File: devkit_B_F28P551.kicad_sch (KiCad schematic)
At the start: 4 parts, among them J1 DEVKIT_C2000_ROW_A, J2 DEVKIT_C2000_ROW_B, J3 JTAG_CTBP_10, U1 TMS320F28P551SG5PM

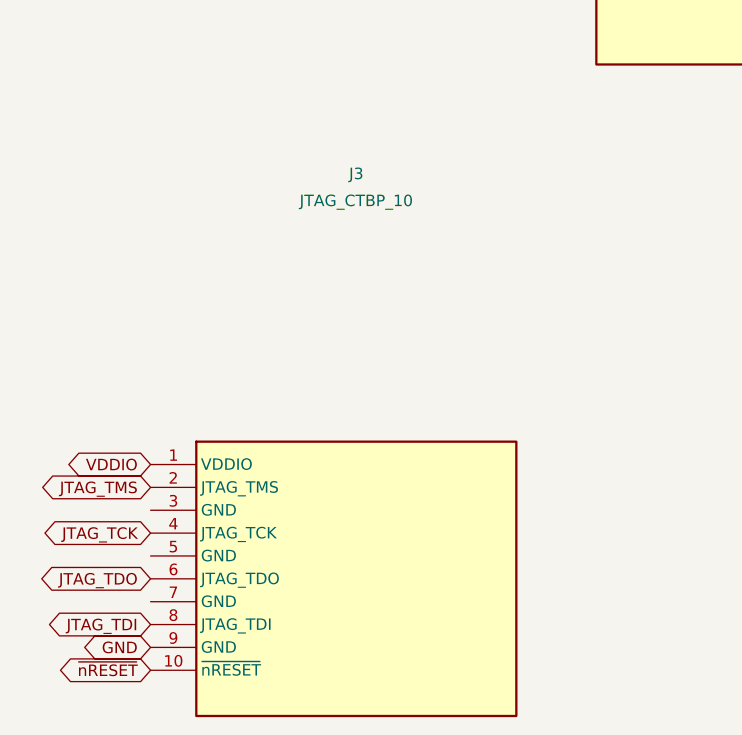
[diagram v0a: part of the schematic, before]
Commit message: Sauvegarde du travail en cours: TC2050 pose a la main dans devkit_B
Point de reprise avant d'ajouter les composants. Le TC2050 a ete ajoute
directement dans le schema genere, que la decision 9 declare jetable: sans ce
commit, le prochain gen_devkit.py --force l'effacait.

Co-Authored-By: Claude Opus 5 <noreply@anthropic.com>
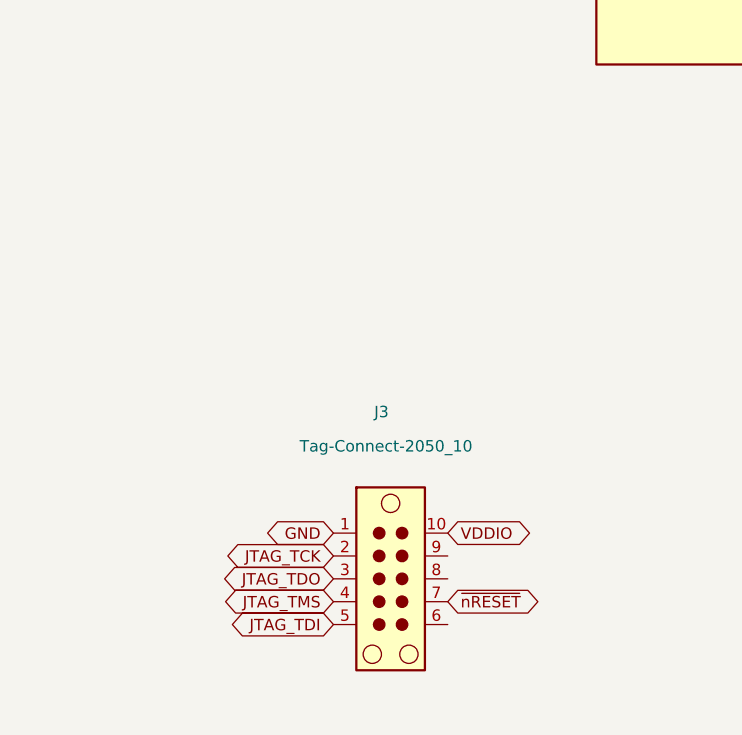
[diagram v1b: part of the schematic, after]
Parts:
- J3: value JTAG_CTBP_10 -> Tag-Connect-2050_10; footprint (none) -> Connector:Tag-Connect_TC2050-IDC-NL_2x05_P1.27mm_Vertical; symbol C2000_Devkit_Connectors:JTAG_CTBP_10 -> Connector:TC2050; now left out of the parts list
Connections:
- net GND: now also J3.1; no longer J3.9 (GND)
- net JTAG_TCK: now also J3.2; no longer J3.4 (JTAG_TCK)
- net JTAG_TDI: now also J3.5; no longer J3.8 (JTAG_TDI)
- net JTAG_TDO: now also J3.3; no longer J3.6 (JTAG_TDO)
- net JTAG_TMS: now also J3.4; no longer J3.2 (JTAG_TMS)
- net VDDIO: now also J3.10; no longer J3.1 (VDDIO)
- net ~{nRESET}: now also J3.7; no longer J3.10 (~{nRESET})

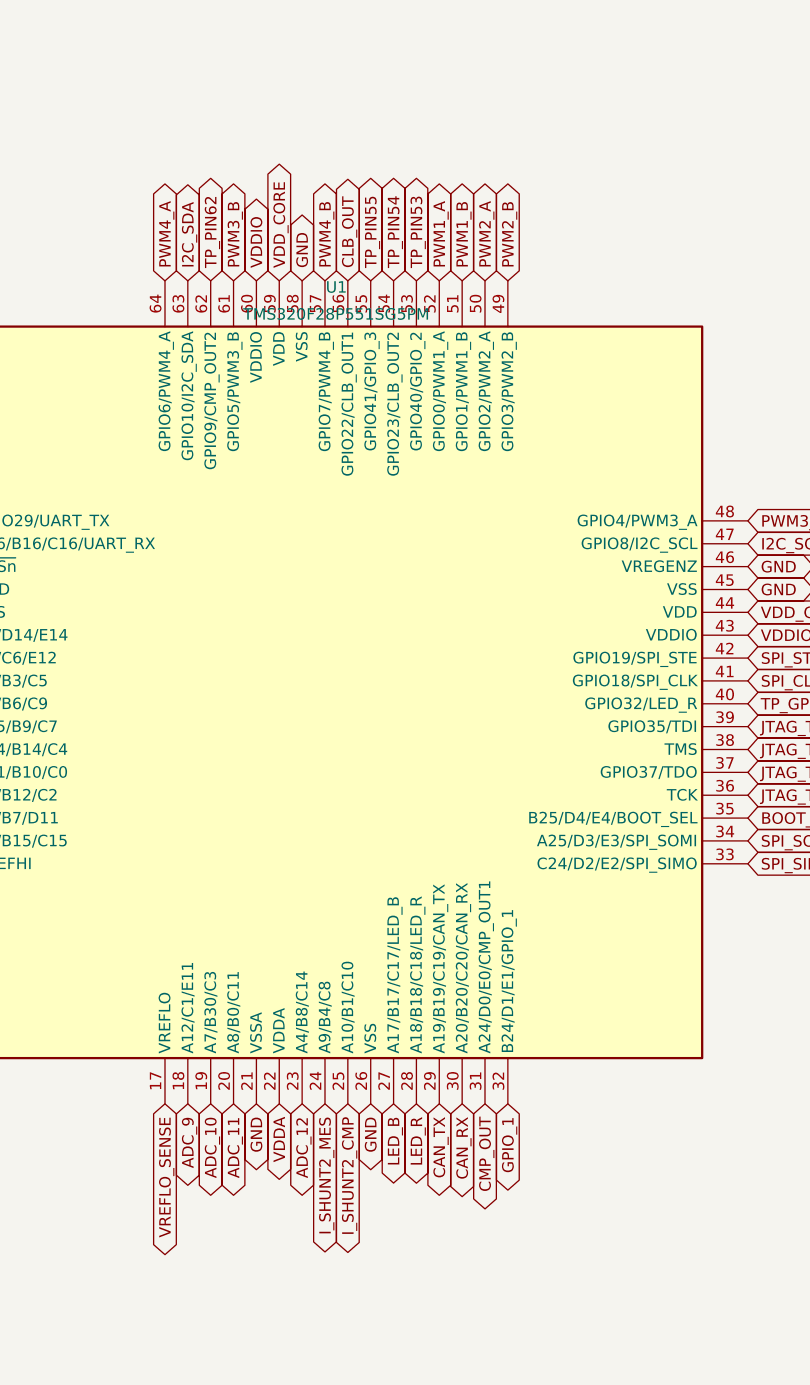
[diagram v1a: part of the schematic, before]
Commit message: LED reportees sur GPIO40 et GPIO23, les deux broches les moins dotees
GPIO32 doit valoir 1 au boot dans les deux modes retenus — Flash (1 1) et SCI
(0 1), ce dernier etant le chemin de mise a jour par l'ESP32. Une LED l'aurait
tenue vers 2,1 V, sous le VIH, cassant les deux d'un coup. GPIO39 part avec.

Broches d'accueil choisies au nombre de fonctions alternatives sacrifiees:
GPIO23 en a 7, GPIO40 en a 9, contre 12 pour GPIO9 qu'on garde libre. Elles
sont communes aux deux boitiers, donc les LED deviennent identiques sur A et B.

Les anciennes positions deviennent des pastilles, differentes par variante:
broches 46 et 40 sur le PCB A, 27 et 28 sur le PCB B.

gen_composants.py est verse au depot mais marque inutilisable: il calcule juste
et produit un fichier que KiCad refuse de charger. Cause isolee a l'insertion
des blocs lib_symbols, reproduite avec un seul Device:R et sans instance.

Co-Authored-By: Claude Opus 5 <noreply@anthropic.com>
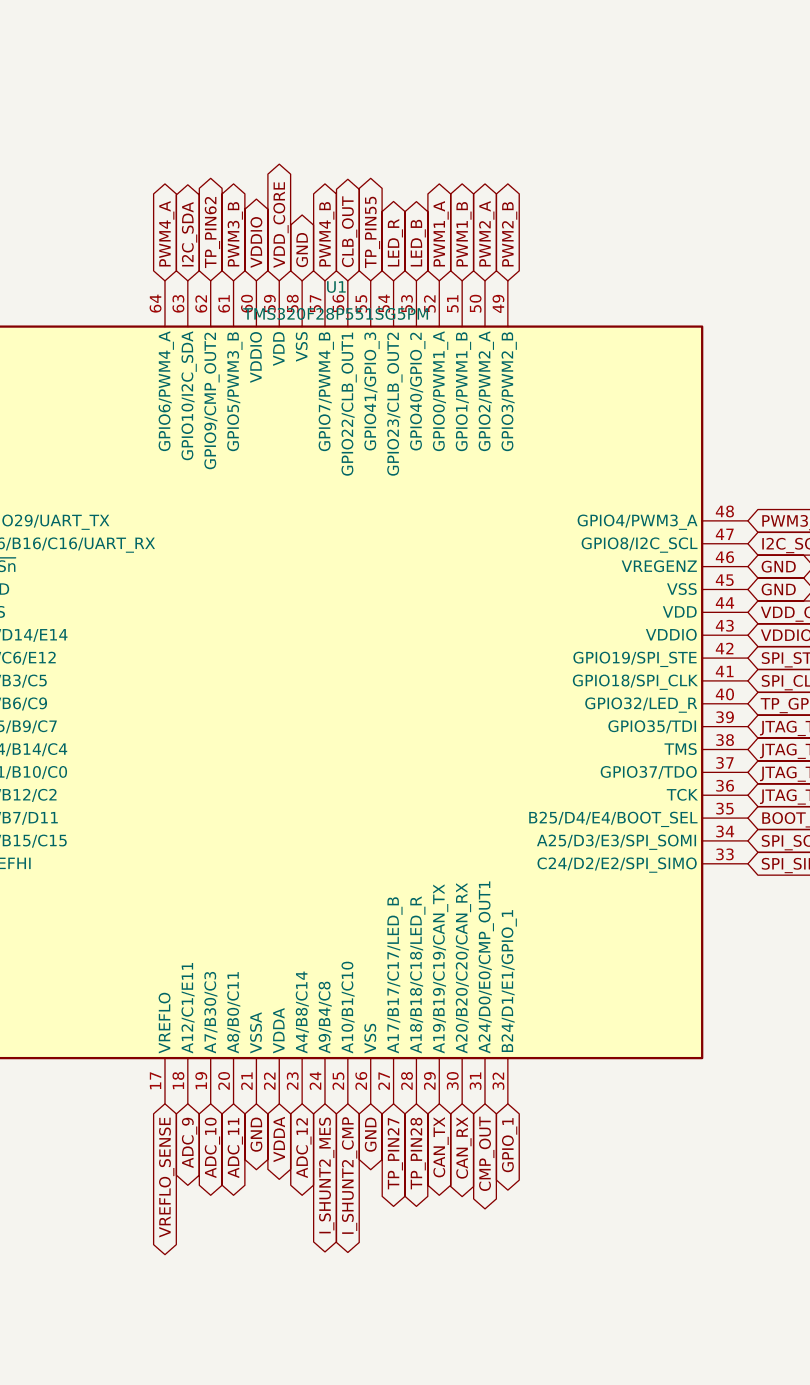
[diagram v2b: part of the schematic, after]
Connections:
- net TP_PIN53 is gone; now on net LED_B: U1.53 (GPIO40/GPIO_2)
- net TP_PIN54 is gone; now on net LED_R: U1.54 (GPIO23/CLB_OUT2)
- net LED_B: no longer U1.27 (A17/B17/C17/LED_B)
- net LED_R: no longer U1.28 (A18/B18/C18/LED_R)
- new net TP_PIN27: U1.27 (A17/B17/C17/LED_B)
- new net TP_PIN28: U1.28 (A18/B18/C18/LED_R)

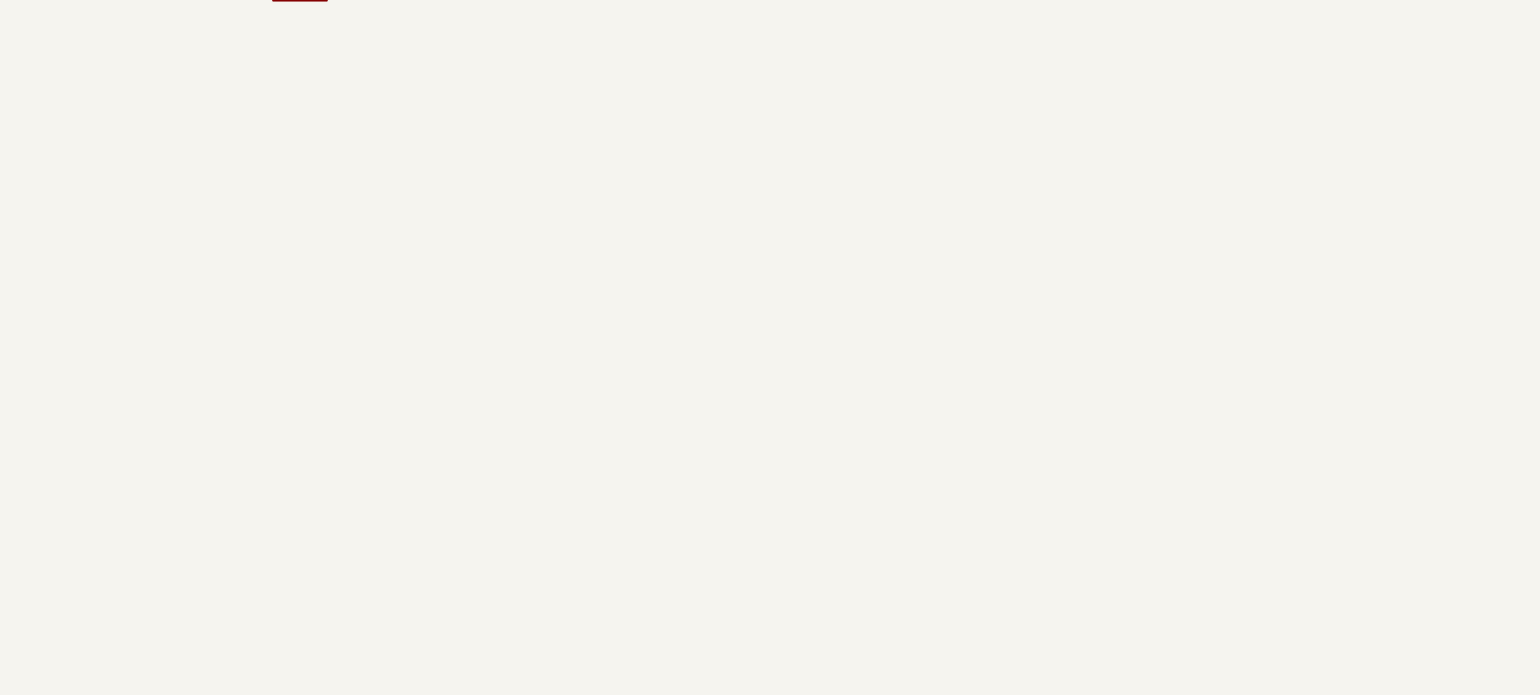
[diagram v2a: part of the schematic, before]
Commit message: Pose les 23 composants dans les deux schemas devkit
Le generateur produisait un fichier que KiCad refusait de charger. Trois
defauts, trouves par bissection puis par diff contre un bloc que KiCad avait
lui-meme ecrit:

1. Dans un schema, seul le symbole de premier niveau porte le prefixe de
   librairie. Ses sous-unites gardent le nom nu — "TC2050_1_1", pas
   "Connector:TC2050_1_1". Les prefixer aussi suffit a rendre le fichier
   illisible, sans autre diagnostic qu'un « echec du chargement ».
2. L'origine de placement n'etait pas un multiple de 1,27 mm: 23 broches hors
   grille, un endpoint_off_grid par composant.
3. Une variante declaree par (extends ...) n'herite que de la geometrie. Sans
   reporter ses propres proprietes sur le bloc de l'ancetre, le symbole pose
   differe de celui que KiCad recalcule et l'ERC leve lib_symbol_mismatch.

ERC apres coup: aucune violation nouvelle sur les deux cartes.

Co-Authored-By: Claude Opus 5 <noreply@anthropic.com>
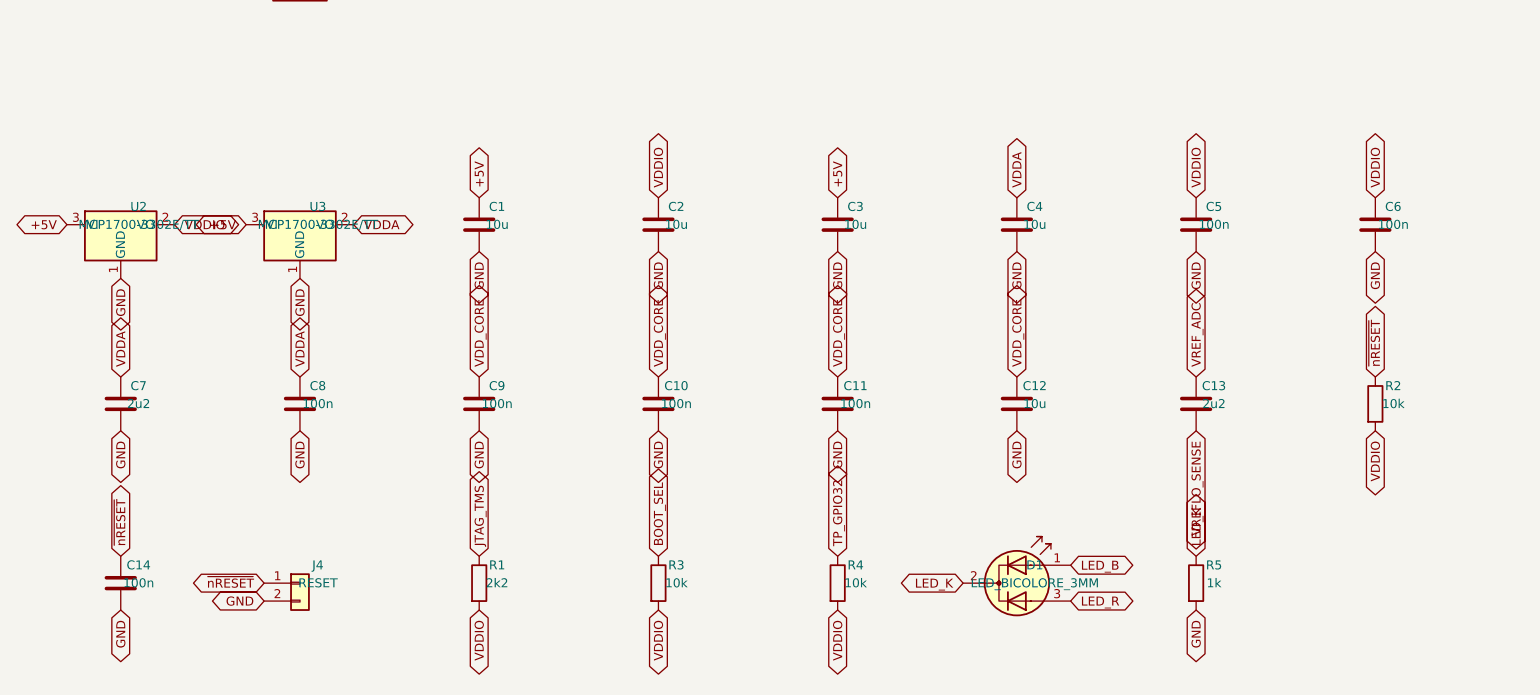
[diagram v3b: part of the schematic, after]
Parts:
- added C1, C12, C2, C3, C4: 10u, Capacitor_SMD:C_0805_2012Metric, symbol Device:C
- added C10, C11, C14, C5, C6, C8, C9: 100n, Capacitor_SMD:C_0805_2012Metric, symbol Device:C
- added C13, C7: 2u2, Capacitor_SMD:C_0805_2012Metric, symbol Device:C
- added D1: LED_BICOLORE_3MM, LED_THT:LED_D3.0mm-3, symbol Device:LED_Dual_AKA
- added J4: RESET, Connector_PinHeader_2.54mm:PinHeader_1x02_P2.54mm_Vertical, symbol Connector_Generic:Conn_01x02
- added R1: 2k2, Resistor_SMD:R_0805_2012Metric, symbol Device:R
- added R2, R3, R4: 10k, Resistor_SMD:R_0805_2012Metric, symbol Device:R
- added R5: 1k, Resistor_SMD:R_0805_2012Metric, symbol Device:R
- added U2, U3: MCP1700-3302E/TT, Package_TO_SOT_SMD:SOT-23, symbol Regulator_Linear:MCP1700x-330xxTT
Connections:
- net +5V: now also C1.1, C3.1, U2.3 (VI), U3.3 (VI)
- net BOOT_SEL: now also R3.1
- net GND: now also C1.2, C10.2, C11.2, C12.2, C14.2, C2.2, C3.2, C4.2, C5.2, C6.2, C7.2, C8.2, C9.2, J4.2 (Pin_2), R5.2, U2.1 (GND), U3.1 (GND)
- net JTAG_TMS: now also R1.1
- net LED_B: now also D1.1 (A1)
- net LED_R: now also D1.3 (A2)
- net TP_GPIO32: now also R4.1
- net VDDA: now also C4.1, C7.1, C8.1, U3.2 (VO)
- net VDDIO: now also C2.1, C5.1, C6.1, R1.2, R2.2, R3.2, R4.2, U2.2 (VO)
- net VDD_CORE: now also C10.1, C11.1, C12.1, C9.1
- net VREFLO_SENSE: now also C13.2
- net VREF_ADC: now also C13.1
- net ~{nRESET}: now also C14.1, J4.1 (Pin_1), R2.1
- new net LED_K: D1.2 (K), R5.1
